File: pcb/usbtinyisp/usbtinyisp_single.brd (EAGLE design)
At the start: 57.1 x 35.8 mm, 20 parts, among them IC1 ATTINY2313-20P, IC2 74AHC125N

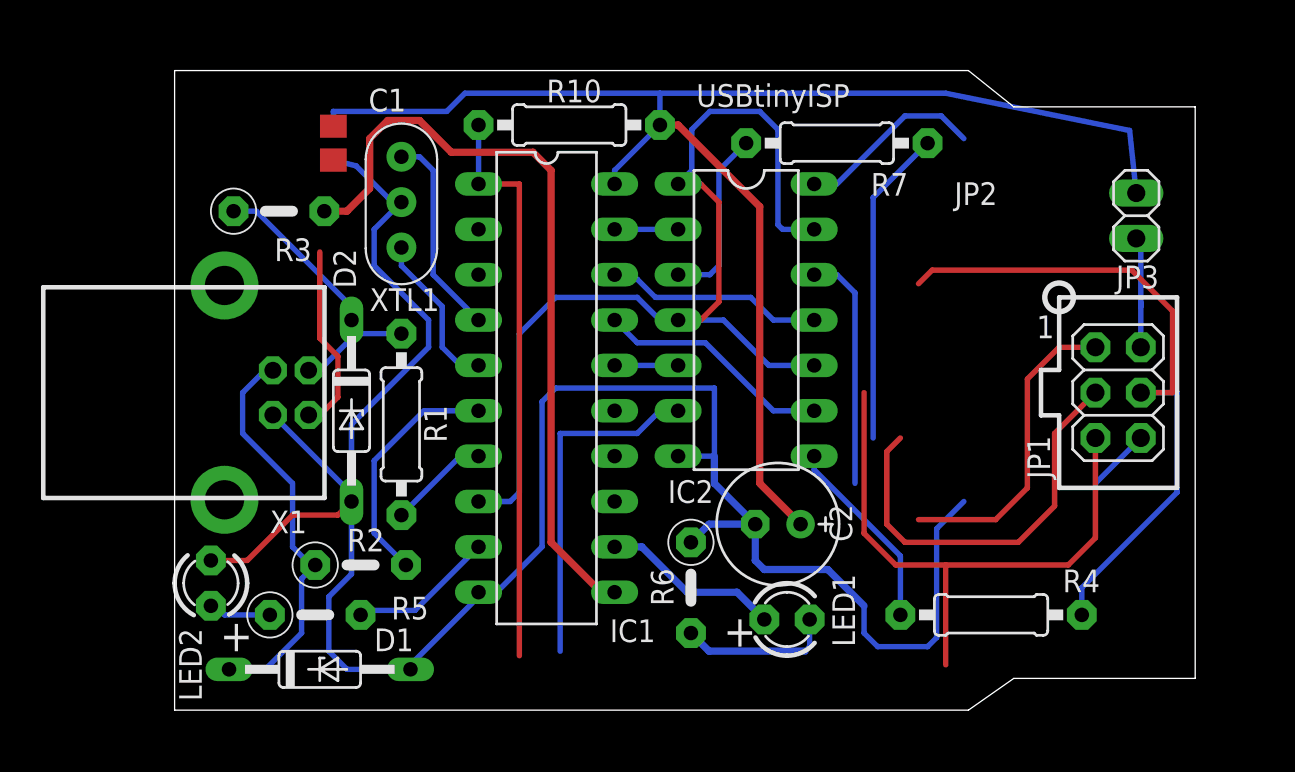
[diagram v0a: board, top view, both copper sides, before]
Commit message: update dimensions and change some packages
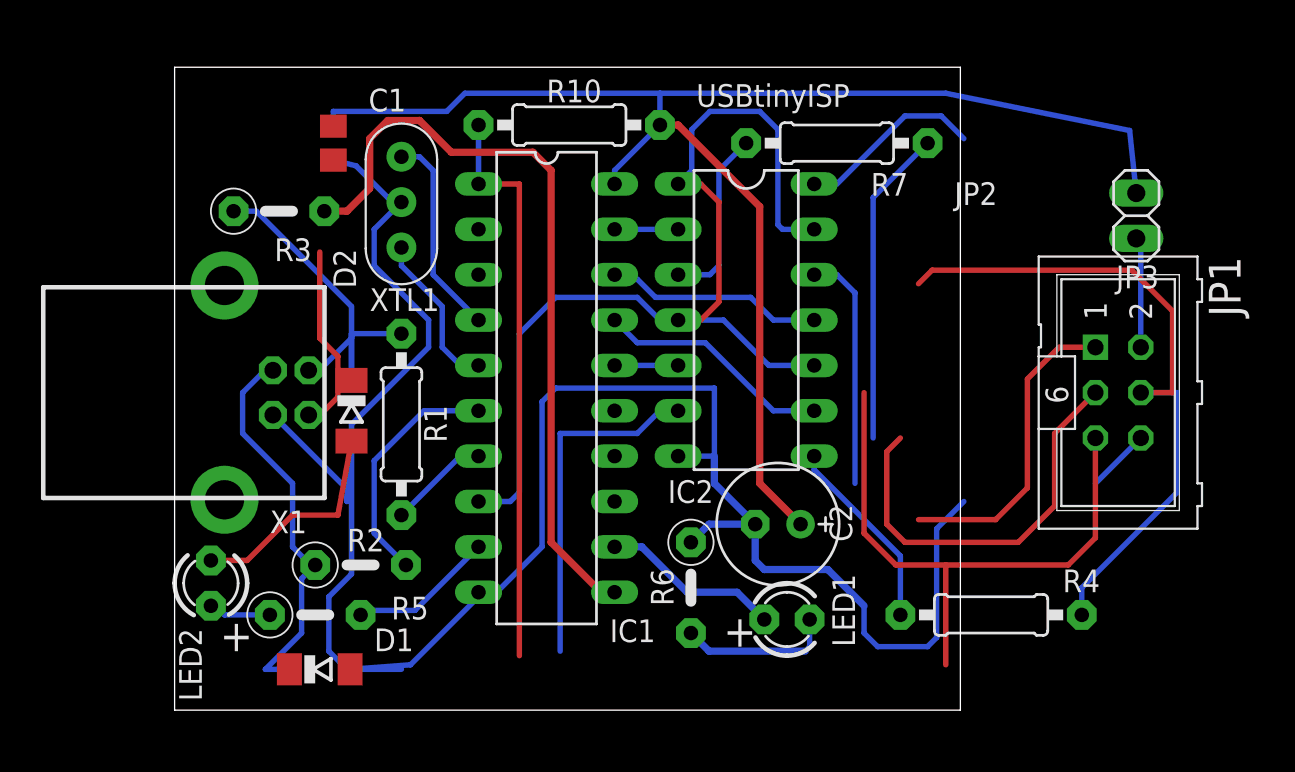
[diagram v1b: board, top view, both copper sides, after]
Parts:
- D1, D2: value 3.6V -> 3V6; device diode:DO35Z10 -> diode:SOD80C
- JP1: device pinhead-ez:2X03 -> con-ml:ML6
- R1, R2: value 27 -> 68
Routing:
- net GND: track 125.9 -> 134.5 mm
- net N$1: track 16.5 -> 21.8 mm
- net N$2: track 22.7 -> 22.0 mm
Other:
- board size 57.1 x 35.8 mm -> 44 x 36 mm
- board text removed: "1"
- board text removed: "JP1"

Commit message: unsmash
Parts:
- C1: value 0.1uF -> 100n
- C2: value 100uF -> 100u
- R10: value 10K -> 10k
- R3, R4, R5, R6, R7: value 1.5K -> 1k5
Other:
- board text removed: "+"
- board text removed: "C1"
- board text removed: "D1"
- board text removed: "D2"
- board text removed: "IC1"
- board text removed: "IC2"
- board text removed: "JP2"
- board text removed: "JP3"
- board text removed: "LED1"
- board text removed: "LED2"
- board text removed: "R1"
- board text removed: "R10"
- board text removed: "R2"
- board text removed: "R3"
- board text removed: "R4"
- board text removed: "R5"
- board text removed: "R6"
- board text removed: "R7"
- board text removed: "X1"
- board text removed: "XTL1"
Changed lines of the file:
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@@
 <setting verticaltext="up"/>
 </settings>
-<grid distance="100" unitdist="mil" unit="mil" style="lines" multiple="1" display="yes" altdistance="0.025" altunitdist="inch" altunit="mil"/>
+<grid distance="100" unitdist="mil" unit="mil" style="lines" multiple="1" display="no" altdistance="0.025" altunitdist="inch" altunit="mil"/>
 <layers>
 <layer number="1" name="Top" color="4" fill="1" visible="yes" active="yes"/>
@@
 <text x="6.096" y="29.718" size="1.016" layer="22" font="vector" rot="MR270">external</text>
 <text x="5.334" y="30.48" size="1.016" layer="22" font="vector" rot="MR90">power</text>
-<text x="5.588" y="25.146" size="1.27" layer="21" font="vector">R3</text>
-<text x="15.24" y="14.986" size="1.27" layer="21" font="vector" rot="R90">R1</text>
-<text x="12.954" y="34.798" size="1.27" layer="21" font="vector" rot="R180">C1</text>
-<text x="11.176" y="3.302" size="1.27" layer="21" font="vector">D1</text>
-<text x="10.16" y="23.622" size="1.27" layer="21" font="vector" rot="R90">D2</text>
-<text x="10.922" y="22.352" size="1.27" layer="21" font="vector">XTL1</text>
-<text x="5.334" y="9.906" size="1.27" layer="21" font="vector">X1</text>
-<text x="36.83" y="7.62" size="1.27" layer="21" font="vector" rot="R270">LED1</text>
-<text x="1.524" y="0.508" size="1.27" layer="21" font="vector" rot="R90">LED2</text>
-<text x="51.816" y="7.874" size="1.27" layer="21" font="vector" rot="R180">R4</text>
-<text x="14.224" y="6.35" size="1.27" layer="21" font="vector" rot="R180">R5</text>
-<text x="27.94" y="5.842" size="1.27" layer="21" font="vector" rot="R90">R6</text>
-<text x="38.9865" y="28.8061" size="1.27" layer="21" font="vector">R7</text>
-<text x="20.828" y="34.036" size="1.27" layer="21" font="vector">R10</text>
-<text x="9.652" y="8.89" size="1.27" layer="21" font="vector">R2</text>
-<text x="46.068" y="29.558" size="1.27" layer="21" font="vector" rot="R180">JP2</text>
-<text x="55.118" y="24.892" size="1.27" layer="21" font="vector" rot="R180">JP3</text>
-<text x="26.924" y="5.08" size="1.27" layer="21" font="vector" rot="R180">IC1</text>
 <text x="21.59" y="9.906" size="1.27" layer="22" font="vector" rot="MR90">www.ladyada.net/</text>
 <text x="19.558" y="11.684" size="1.27" layer="22" font="vector" rot="MR90">make/usbtiny</text>
 <text x="29.21" y="33.782" size="1.27" layer="21" font="vector">USBtinyISP</text>
-<text x="30.734" y="3.556" size="1.778" layer="21" font="vector">+</text>
-<text x="27.61741875" y="11.60271875" size="1.27" layer="21" font="vector">IC2</text>
-<text x="2.54" y="3.302" size="1.778" layer="21" font="vector">+</text>
 </plain>
 <attributes>
@@
 </autorouter>
 <elements>
-<element name="R1" library="rcl-ez" package="0207/10" value="68" x="12.7" y="16.002" smashed="yes" rot="R270">
-<attribute name="VALUE" x="14.605" y="20.2946" size="1.27" layer="27" ratio="10" rot="R270"/>
-</element>
-<element name="R2" library="rcl-ez" package="0207/5V" value="68" x="10.414" y="8.128" smashed="yes">
-<attribute name="VALUE" x="4.5466" y="9.525" size="1.27" layer="27" ratio="10" rot="R180"/>
-</element>
-<element name="R3" library="rcl-ez" package="0207/5V" value="1.5K" x="5.842" y="27.94" smashed="yes">
-<attribute name="VALUE" x="3.8354" y="27.305" size="1.27" layer="27" ratio="10"/>
-</element>
-<element name="XTL1" library="minimidi" package="CERM_OSC" value="12.0 MHz" x="12.7" y="28.448" smashed="yes" rot="R270">
-<attribute name="VALUE" x="10.486" y="31.948" size="1.27" layer="27" rot="R270"/>
-</element>
-<element name="IC1" library="avr" package="DIL20" value="ATTINY2313-20P" x="20.828" y="18.034" smashed="yes" rot="R270">
-<attribute name="VALUE" x="20.066" y="28.194" size="1.778" layer="27" ratio="10" rot="R270"/>
-</element>
-<element name="JP3" library="pinhead" package="1X02" value="PWR" x="53.848" y="27.686" smashed="yes" rot="R90">
-<attribute name="VALUE" x="57.023" y="25.146" size="1.27" layer="27" rot="R90"/>
-</element>
-<element name="C1" library="rcl" package="C0805" value="0.1uF" x="8.89" y="31.75" smashed="yes" rot="R270">
-<attribute name="VALUE" x="10.668" y="33.528" size="1.27" layer="27" ratio="10" rot="R270"/>
-</element>
-<element name="LED1" library="minimidi" package="LED3MM" value="" x="34.29" y="5.08" smashed="yes">
-<attribute name="VALUE" x="36.195" y="3.429" size="1.27" layer="27" ratio="10"/>
-</element>
-<element name="R6" library="rcl-ez" package="0207/5V" value="1.5K" x="28.9123" y="6.858" smashed="yes" rot="R270">
-<attribute name="VALUE" x="28.2773" y="9.1186" size="1.27" layer="27" ratio="10" rot="R270"/>
-</element>
-<element name="D1" library="diode" package="SOD80C" value="3V6" x="8.128" y="2.286" smashed="yes">
-<attribute name="VALUE" x="1.524" y="1.27" size="1.27" layer="27" ratio="10" rot="R90"/>
-</element>
-<element name="D2" library="diode" package="SOD80C" value="3V6" x="9.906" y="16.764" smashed="yes" rot="R270">
-<attribute name="VALUE" x="5.588" y="10.414" size="1.27" layer="27" ratio="10"/>
-</element>
-<element name="R7" library="rcl-ez" package="0207/10" value="1.5K" x="37.084" y="31.75" smashed="yes" rot="R180">
-<attribute name="VALUE" x="41.275" y="32.639" size="1.27" layer="27" ratio="10" rot="R270"/>
-</element>
-<element name="R4" library="rcl-ez" package="0207/10" value="1.5K" x="45.72" y="5.334" smashed="yes" rot="R180">
-<attribute name="VALUE" x="46.863" y="7.493" size="1.27" layer="27" ratio="10" rot="R180"/>
-</element>
-<element name="R10" library="rcl-ez" package="0207/10" value="10K" x="22.098" y="32.766" smashed="yes">
-<attribute name="VALUE" x="20.955" y="30.607" size="1.27" layer="27" ratio="10"/>
-</element>
-<element name="R5" library="rcl-ez" package="0207/5V" value="1.5K" x="7.874" y="5.334" smashed="yes">
-<attribute name="VALUE" x="5.6134" y="4.699" size="1.27" layer="27" ratio="10"/>
-</element>
-<element name="LED2" library="minimidi" package="LED3MM" value="" x="2.032" y="7.112" smashed="yes" rot="R90">
-<attribute name="VALUE" x="3.683" y="9.017" size="1.27" layer="27" ratio="10" rot="R90"/>
-</element>
+<element name="R1" library="rcl-ez" package="0207/10" value="68" x="12.7" y="16.002" rot="R270"/>
+<element name="R2" library="rcl-ez" package="0207/5V" value="68" x="10.414" y="8.128"/>
+<element name="R3" library="rcl-ez" package="0207/5V" value="1k5" x="5.842" y="27.94"/>
+<element name="XTL1" library="minimidi" package="CERM_OSC" value="12.0 MHz" x="12.7" y="28.448" rot="R270"/>
+<element name="IC1" library="avr" package="DIL20" value="ATTINY2313-20P" x="20.828" y="18.034" rot="R270"/>
+<element name="JP3" library="pinhead" package="1X02" value="PWR" x="53.848" y="27.686" rot="R90"/>
+<element name="C1" library="rcl" package="C0805" value="100n" x="8.89" y="31.75" rot="R270"/>
+<element name="LED1" library="minimidi" package="LED3MM" value="" x="34.29" y="5.08"/>
+<element name="R6" library="rcl-ez" package="0207/5V" value="1k5" x="28.9123" y="6.858" rot="R270"/>
+<element name="D1" library="diode" package="SOD80C" value="3V6" x="8.128" y="2.286"/>
+<element name="D2" library="diode" package="SOD80C" value="3V6" x="9.906" y="16.764" rot="R270"/>
+<element name="R7" library="rcl-ez" package="0207/10" value="1k5" x="37.084" y="31.75" rot="R180"/>
+<element name="R4" library="rcl-ez" package="0207/10" value="1k5" x="45.72" y="5.334" rot="R180"/>
+<element name="R10" library="rcl-ez" package="0207/10" value="10k" x="22.098" y="32.766"/>
+<element name="R5" library="rcl-ez" package="0207/5V" value="1k5" x="7.874" y="5.334"/>
+<element name="LED2" library="minimidi" package="LED3MM" value="" x="2.032" y="7.112" rot="R90"/>
 <element name="JP1" library="con-ml" package="ML6" value="" x="52.832" y="17.78" rot="R270">
 <attribute name="OC_NEWARK" value="unknown" x="52.832" y="17.78" size="1.778" layer="27" rot="R270" display="off"/>
@@
 <attribute name="OC_FARNELL" value="unknown" x="52.832" y="17.78" size="1.778" layer="27" rot="R270" display="off"/>
 </element>
-<element name="X1" library="con-berg-ez" package="PN61729" value="" x="2.794" y="17.78" smashed="yes" rot="R270">
-<attribute name="VALUE" x="-6.096" y="10.16" size="1.27" layer="27"/>
-</element>
-<element name="IC2" library="74xx-eu" package="DIL14" value="74AHC125N" x="32.004" y="21.844" smashed="yes" rot="R270">
-<attribute name="VALUE" x="31.369" y="28.575" size="1.27" layer="27" ratio="10" rot="R270"/>
-</element>
-<element name="C2" library="rcl" package="E2,5-7" value="100uF" x="33.782" y="10.414" smashed="yes" rot="R180">
-<attribute name="NAME" x="36.675" y="11.5189" size="1.27" layer="25" font="vector" ratio="10" rot="R270"/>
-<attribute name="VALUE" x="31.369" y="12.827" size="1.27" layer="27" ratio="10" rot="R180"/>
-</element>
+<element name="X1" library="con-berg-ez" package="PN61729" value="" x="2.794" y="17.78" rot="R270"/>
+<element name="IC2" library="74xx-eu" package="DIL14" value="74AHC125N" x="32.004" y="21.844" rot="R270"/>
+<element name="C2" library="rcl" package="E2,5-7" value="100u" x="33.782" y="10.414" rot="R180"/>
 </elements>
 <signals>
@@
 <wire x1="28.194" y1="32.766" x2="32.766" y2="28.194" width="0.4064" layer="1"/>
 <wire x1="27.178" y1="32.766" x2="28.194" y2="32.766" width="0.4064" layer="1"/>
+<wire x1="8.89" y1="32.7" x2="8.89" y2="32.7" width="0" layer="19" extent="1-16"/>
 <wire x1="8.128" y1="25.654" x2="8.89" y2="32.7" width="0" layer="19" extent="1-1"/>
 </signal>

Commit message: vergessene Änderungen
wenn man nicht alles gleich commited :-/
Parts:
- removed XTL1: 12.0 MHz, minimidi:CERM_OSC
- added C3, C4: 22p, rcl:C1206
- added Q1: 12000, crystal:HC49U-V
- added U$1, U$2, U$3, U$4: (no value), holes:3,2
- IC2: value 74AHC125N -> 74LVX125D; device 74xx-eu:DIL14 -> 74xx-eu:SO14
- R1, R10, R4, R7: device rcl-ez:0207/10 -> rcl:R0805
- R2, R3, R5, R6: device rcl-ez:0207/5V -> rcl:R0805
- moved R3 26.5 mm to (22.9, 7.62), flipped to the bottom, turned to 180 degrees
- moved LED2 21.3 mm to (22.9, 2.54)
- moved R4 18.7 mm to (31.8, 17.8), flipped to the bottom, turned to 0 degrees
- moved C2 17.7 mm to (16.5, 6.35)
- moved C1 17.3 mm to (22.9, 21.6), flipped to the bottom
- moved R5 16.2 mm to (22.9, 11.4), flipped to the bottom, turned to 180 degrees
- moved JP1 14.9 mm to (38.1, 15.2)
- moved JP3 13.4 mm to (40.6, 25.4), turned to 180 degrees
- moved IC2 6.18 mm to (33.0, 27.9), flipped to the bottom
- moved LED1 5.68 mm to (29.2, 2.54)
- moved R7 5.21 mm to (40.6, 27.9), flipped to the bottom, turned to 0 degrees
- moved IC1 4.10 mm to (22.9, 21.6)
- moved D2 3.18 mm to (12.7, 15.2), flipped to the bottom
- moved R6 2.88 mm to (31.8, 6.35), flipped to the bottom
- moved R1 2.65 mm to (15.2, 15.2), flipped to the bottom
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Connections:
- removed net N$4: IC1.5, XTL1.P$3
- removed net N$5: IC1.4, XTL1.P$1
- new net XTAL1: C4.1, IC1.5, Q1.1
- new net XTAL2: C3.1, IC1.4, Q1.2
- net GND: now also C3.2, C4.2; no longer XTL1.P$2
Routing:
- net GND: track 134.5 -> 0.00 mm
- net VCC: track 92.5 -> 0.00 mm
- net N$15: track 58.3 -> 0.00 mm
- net RST: track 52.7 -> 0.00 mm
- net N$16: track 43.4 -> 0.00 mm
- net SCK: track 40.9 -> 0.00 mm
- net MOSI: track 38.5 -> 0.00 mm
- net N$9: track 32.0 -> 0.00 mm
- net MISO: track 30.8 -> 0.00 mm
- net N$2: track 22.0 -> 0.00 mm
- net N$1: track 21.8 -> 0.00 mm
- net N$14: track 17.1 -> 0.00 mm
- net N$6: track 13.6 -> 0.00 mm
- net MOSI': track 13.5 -> 0.00 mm
- net MISO': track 12.2 -> 0.00 mm
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- added copper zone on layer 16, net GND
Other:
- board text removed: "AVR"
- board text removed: "Dongle"
- board text removed: "GND"
- board text removed: "MISO"
- board text removed: "MOSI"
- board text removed: "N/C"
- board text removed: "RST"
- board text removed: "SCK"
- board text removed: "SpokePOV"
- board text removed: "USB"
- board text removed: "USBtiny"
- board text removed: "USBtinyISP"
- board text removed: "VCC"
- board text removed: "cut to use"
- board text removed: "external"
- board text removed: "make/usbtiny"
- board text removed: "power"
- board text removed: "programmer"
- board text removed: "www.ladyada.net/"

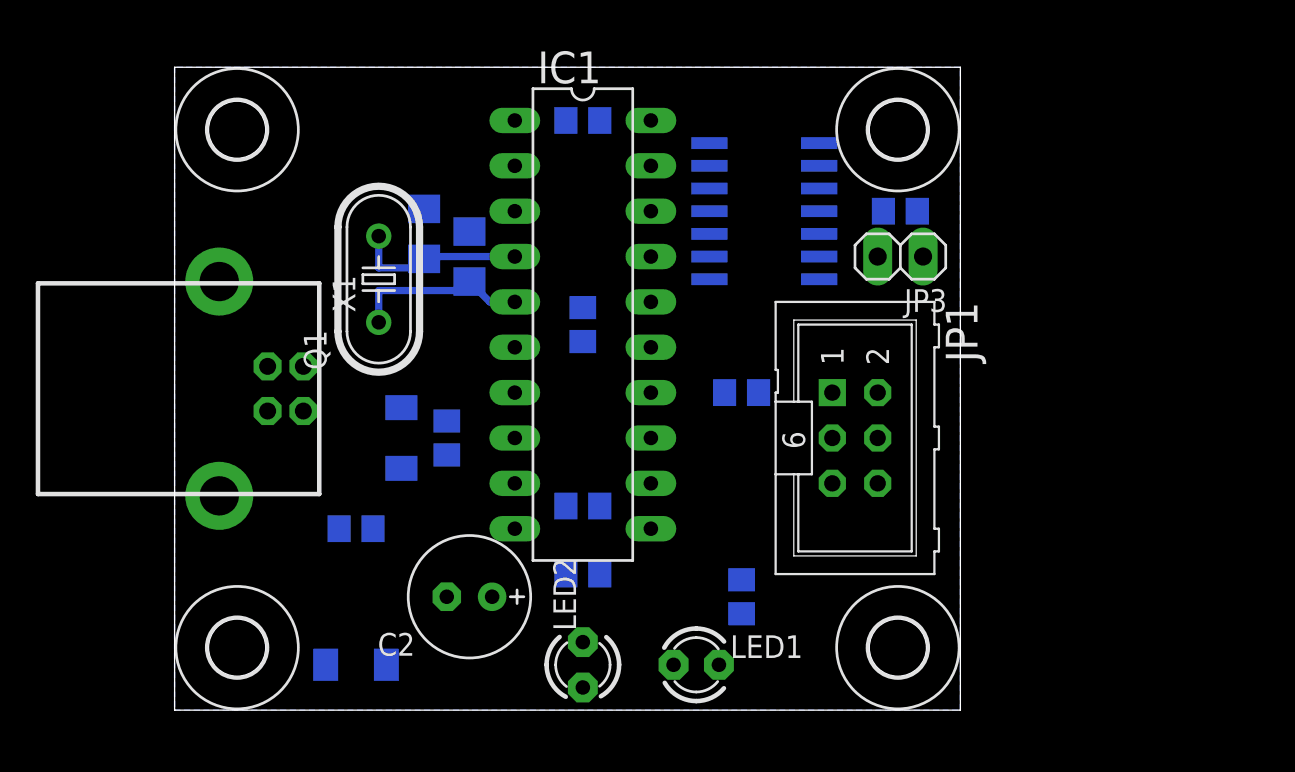
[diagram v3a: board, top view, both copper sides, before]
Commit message: move mounting holes inward
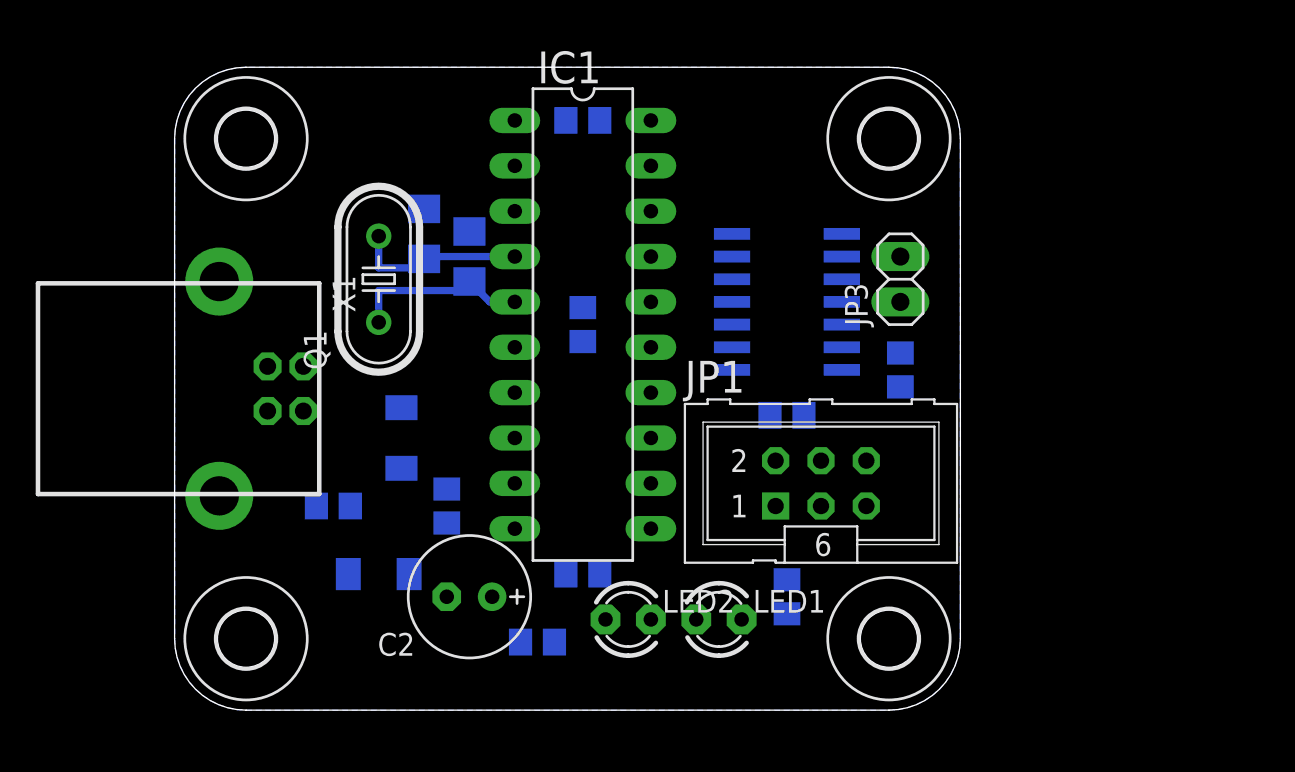
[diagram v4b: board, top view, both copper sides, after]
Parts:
- moved R7 8.89 mm to (40.6, 19.1), turned to 90 degrees
- moved R5 8.03 mm to (20.3, 3.81), turned to 0 degrees
- moved IC2 5.24 mm to (34.3, 22.9)
- moved D1 5.24 mm to (11.4, 7.62), turned to 180 degrees
- moved R1 3.81 mm to (15.2, 11.4), turned to 90 degrees
- moved LED2 3.59 mm to (25.4, 5.08), turned to 0 degrees
- moved JP1 3.18 mm to (36.2, 12.7), turned to 0 degrees
- moved LED1 2.84 mm to (30.5, 5.08)
- moved R4 2.84 mm to (34.3, 16.5)
- moved R6 2.54 mm to (34.3, 6.35)
- moved R2 1.80 mm to (8.89, 11.4)
- moved JP3 1.27 mm to (40.6, 24.1), turned to 90 degrees
- moved U$1 0.71 mm to (4.00, 4.00)
- moved U$2 0.71 mm to (40.0, 4.00)
- moved U$3 0.71 mm to (40.0, 32.0)
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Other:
- outline, holes or cut-outs redrawn
